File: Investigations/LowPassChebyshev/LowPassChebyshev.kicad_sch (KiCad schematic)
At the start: 8 parts

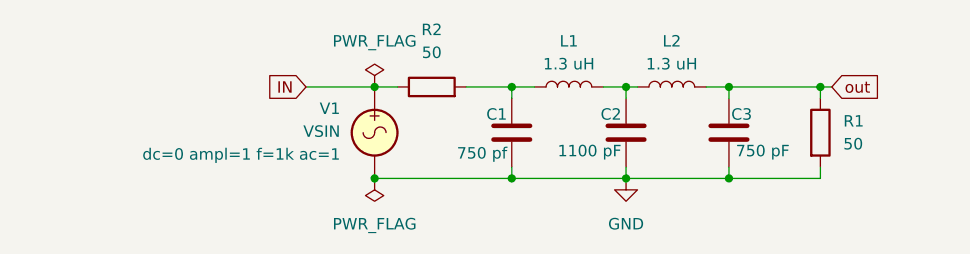
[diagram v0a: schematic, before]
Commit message: Both the main board and filter board submitted to PCBway
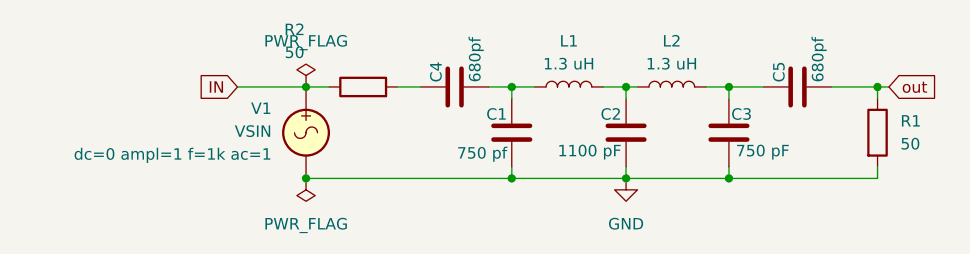
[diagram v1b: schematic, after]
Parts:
- added C4, C5: 680pf, symbol Device:C
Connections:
- net out: now also C5.2; no longer C3.1, L2.2
- net at C1.1, L1.1: now also C4.2; no longer R2.2
- new net: C3.1, C5.1, L2.2
- new net: C4.1, R2.2
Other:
- moved on the sheet: R1, R2, V1
